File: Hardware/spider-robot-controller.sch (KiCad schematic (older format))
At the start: 16 parts, among them CON1 AVR-ISP-6, IC1 ATMEGA328-P, P1 SERVO_HEADER, P10 SERVO_HEADER, P11 SERVO_HEADER, P12 SERVO_HEADER, P2 SERVO_HEADER, P3 SERVO_HEADER, P4 SERVO_HEADER, P5 SERVO_HEADER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

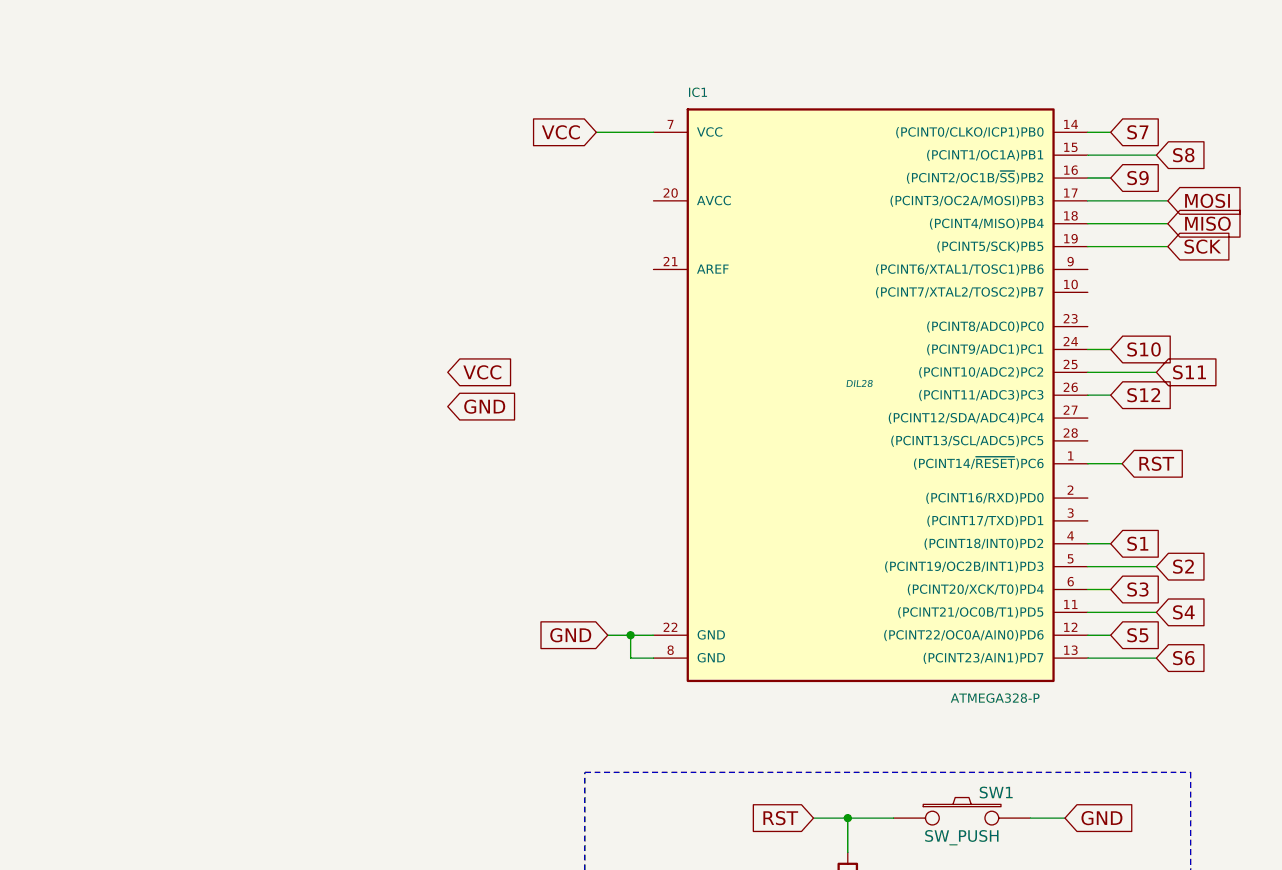
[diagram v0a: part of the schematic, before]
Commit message: Added crystal
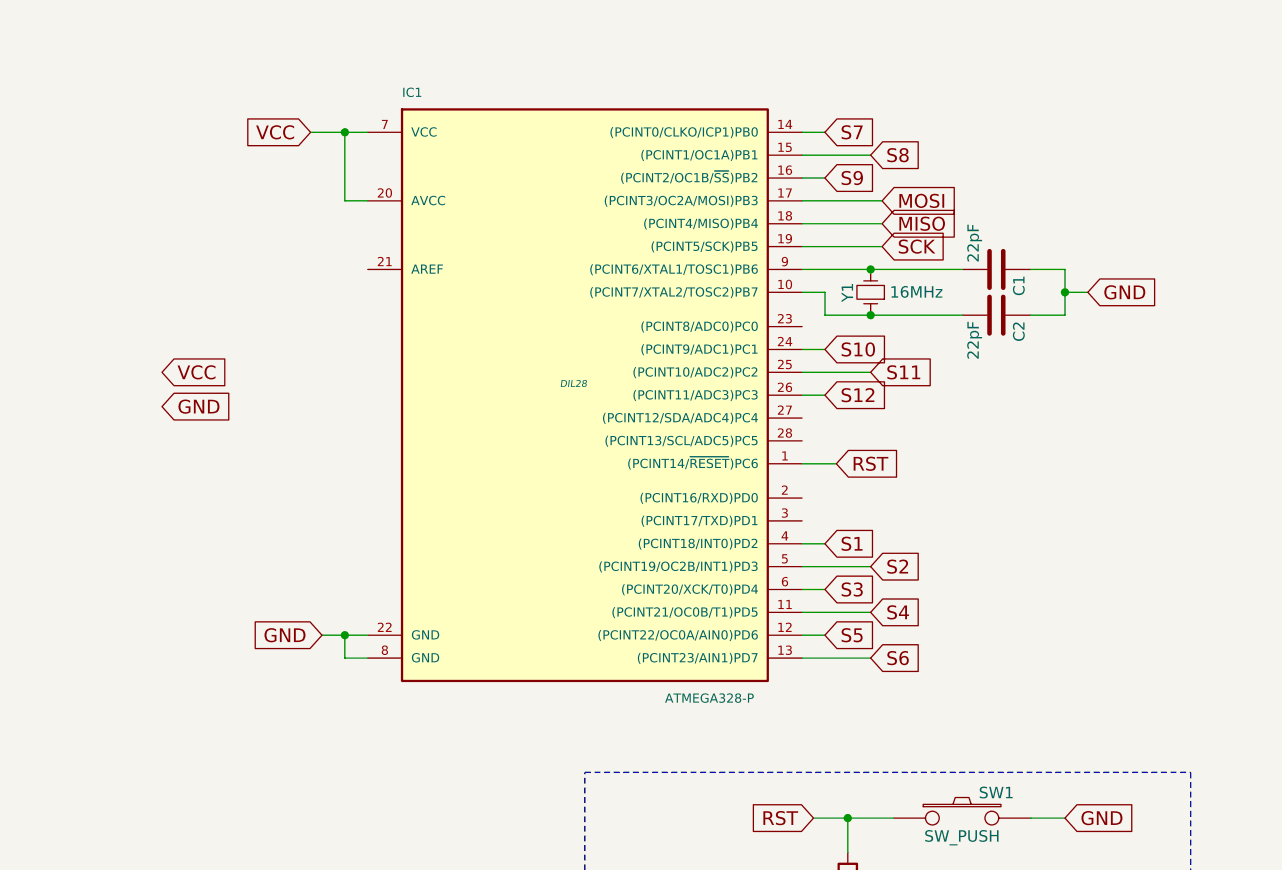
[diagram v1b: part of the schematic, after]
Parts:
- added C1, C2: 22pF, symbol C
- added Y1: 16MHz, symbol Crystal_Small
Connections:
- net GND: now also C1.1, C2.1
- net VCC: now also IC1.20 (AVCC)
- net at IC1.10 ((PCINT7/XTAL2/TOSC2)PB7): now also C2.2, Y1.1
- net at IC1.9 ((PCINT6/XTAL1/TOSC1)PB6): now also C1.2, Y1.2
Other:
- moved on the sheet: IC1
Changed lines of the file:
@@
 L ATMEGA328-P IC1
 U 1 1 55F95AA5
-P 9100 2150
-F 0 "IC1" H 8350 3400 40  0000 L BNN
-F 1 "ATMEGA328-P" H 9500 750 40  0000 L BNN
-F 2 "DIL28" H 9100 2150 30  0000 C CIN
-F 3 "" H 9100 2150 60  0000 C CNN
-	1    9100 2150
+P 7850 2150
+F 0 "IC1" H 7100 3400 40  0000 L BNN
+F 1 "ATMEGA328-P" H 8250 750 40  0000 L BNN
+F 2 "DIL28" H 7850 2150 30  0000 C CIN
+F 3 "" H 7850 2150 60  0000 C CNN
+	1    7850 2150
 	1    0    0    -1
 $EndComp
@@
 Text Notes 9500 6200 0    60   ~ 0
 PROGRAMMER HEADER
-Text GLabel 10250 2500 2    60   Input ~ 0
+Text GLabel 9000 2500 2    60   Input ~ 0
 RST
-Text GLabel 10450 1550 2    60   Input ~ 0
+Text GLabel 9200 1550 2    60   Input ~ 0
 SCK
-Text GLabel 7300 2100 2    60   Input ~ 0
-VCC
-Text GLabel 7300 2250 2    60   Input ~ 0
-GND
-Text GLabel 8000 3250 0    60   Input ~ 0
-GND
-Wire Wire Line
-	8000 3250 8200 3250
-Wire Wire Line
-	8200 3350 8100 3350
-Wire Wire Line
-	8100 3350 8100 3250
-Connection ~ 8100 3250
-Text GLabel 7950 1050 0    60   Input ~ 0
-VCC
-Wire Wire Line
-	7950 1050 8200 1050
+Text GLabel 6050 2100 2    60   Input ~ 0
+VCC
+Text GLabel 6050 2250 2    60   Input ~ 0
+GND
+Text GLabel 6750 3250 0    60   Input ~ 0
+GND
+Wire Wire Line
+	6750 3250 6950 3250
+Wire Wire Line
+	6950 3350 6850 3350
+Wire Wire Line
+	6850 3350 6850 3250
+Connection ~ 6850 3250
+Text GLabel 6700 1050 0    60   Input ~ 0
+VCC
+Wire Wire Line
+	6700 1050 6950 1050
 $Comp
 L SW_PUSH SW1
@@
 RST
 Wire Wire Line
-	10250 2500 10100 2500
+	9000 2500 8850 2500
 Wire Wire Line
 	8900 4050 9250 4050
@@
 RESET CIRCUIT
 Wire Wire Line
-	10100 1550 10450 1550
-Text GLabel 10450 1450 2    60   Input ~ 0
+	8850 1550 9200 1550
+Text GLabel 9200 1450 2    60   Input ~ 0
 MISO
 Wire Wire Line
-	10100 1450 10450 1450
-Text GLabel 10450 1350 2    60   Input ~ 0
+	8850 1450 9200 1450
+Text GLabel 9200 1350 2    60   Input ~ 0
 MOSI
 Wire Wire Line
-	10100 1350 10450 1350
+	8850 1350 9200 1350
 $Comp
 L CONN_01X03 P1
@@
 Text Notes 2800 4100 0    60   ~ 0
 Servo Headers
-Text GLabel 10200 2850 2    60   Input ~ 0
+Text GLabel 8950 2850 2    60   Input ~ 0
 S1
 Wire Wire Line
-	10200 2850 10100 2850
-Text GLabel 10400 2950 2    60   Input ~ 0
+	8950 2850 8850 2850
+Text GLabel 9150 2950 2    60   Input ~ 0
 S2
 Wire Wire Line
-	10400 2950 10100 2950
-Text GLabel 10200 3050 2    60   Input ~ 0
+	9150 2950 8850 2950
+Text GLabel 8950 3050 2    60   Input ~ 0
 S3
 Wire Wire Line
-	10200 3050 10100 3050
-Text GLabel 10400 3150 2    60   Input ~ 0
+	8950 3050 8850 3050
+Text GLabel 9150 3150 2    60   Input ~ 0
 S4
 Wire Wire Line
-	10400 3150 10100 3150
-Text GLabel 10200 3250 2    60   Input ~ 0
+	9150 3150 8850 3150
+Text GLabel 8950 3250 2    60   Input ~ 0
 S5
 Wire Wire Line
-	10200 3250 10100 3250
-Text GLabel 10400 3350 2    60   Input ~ 0
+	8950 3250 8850 3250
+Text GLabel 9150 3350 2    60   Input ~ 0
 S6
 Wire Wire Line
-	10400 3350 10100 3350
-Text GLabel 10200 1050 2    60   Input ~ 0
+	9150 3350 8850 3350
+Text GLabel 8950 1050 2    60   Input ~ 0
 S7
 Wire Wire Line
-	10200 1050 10100 1050
-Text GLabel 10400 1150 2    60   Input ~ 0
+	8950 1050 8850 1050
+Text GLabel 9150 1150 2    60   Input ~ 0
 S8
 Wire Wire Line
-	10400 1150 10100 1150
-Text GLabel 10200 1250 2    60   Input ~ 0
+	9150 1150 8850 1150
+Text GLabel 8950 1250 2    60   Input ~ 0
 S9
 Wire Wire Line
-	10200 1250 10100 1250
-Text GLabel 10200 2000 2    60   Input ~ 0
+	8950 1250 8850 1250
+Text GLabel 8950 2000 2    60   Input ~ 0
 S10
 Wire Wire Line
-	10200 2000 10100 2000
-Text GLabel 10400 2100 2    60   Input ~ 0
+	8950 2000 8850 2000
+Text GLabel 9150 2100 2    60   Input ~ 0
 S11
 Wire Wire Line
-	10400 2100 10100 2100
-Text GLabel 10200 2200 2    60   Input ~ 0
+	9150 2100 8850 2100
+Text GLabel 8950 2200 2    60   Input ~ 0
 S12
 Wire Wire Line
-	10200 2200 10100 2200
+	8950 2200 8850 2200
+Wire Wire Line
+	6950 1350 6850 1350
+Wire Wire Line
+	6850 1350 6850 1050
+Connection ~ 6850 1050
+$Comp
+L Crystal_Small Y1
+U 1 1 55F98E0B
+P 9150 1750
+F 0 "Y1" H 9150 1850 50  0000 C CNN
+F 1 "16MHz" V 9150 1550 50  0000 C CNN
+F 2 "" H 9150 1750 60  0000 C CNN
+F 3 "" H 9150 1750 60  0000 C CNN
+	1    9150 1750
+	0    -1   -1   0
+$EndComp
+Wire Wire Line
+	8850 1650 9550 1650
+Wire Wire Line
+	8850 1750 8950 1750
+Wire Wire Line
+	8950 1750 8950 1850
+Wire Wire Line
+	8950 1850 9550 1850
+Connection ~ 9150 1650
+Connection ~ 9150 1850
+$Comp
+L C C1
+U 1 1 55F9917D
+P 9700 1650
+F 0 "C1" H 9725 1750 50  0000 L CNN
+F 1 "22pF" H 9500 1550 50  0000 L CNN
+F 2 "" H 9738 1500 30  0000 C CNN
+F 3 "" H 9700 1650 60  0000 C CNN
+	1    9700 1650
+	0    1    1    0
+$EndComp
+$Comp
+L C C2
+U 1 1 55F99278
+P 9700 1850
+F 0 "C2" H 9725 1950 50  0000 L CNN
+F 1 "22pF" H 9725 1750 50  0000 L CNN
+F 2 "" H 9738 1700 30  0000 C CNN
+F 3 "" H 9700 1850 60  0000 C CNN
+	1    9700 1850
+	0    1    1    0
+$EndComp
+Text GLabel 10100 1750 2    60   Input ~ 0
+GND
+Wire Wire Line
+	9850 1650 10000 1650
+Wire Wire Line
+	10000 1650 10000 1850
+Wire Wire Line
+	10000 1850 9850 1850
+Wire Wire Line
+	10100 1750 10000 1750
+Connection ~ 10000 1750
 $EndSCHEMATC
